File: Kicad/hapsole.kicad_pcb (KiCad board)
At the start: 2 copper layers, 39.3 x 36.8 mm, 63 parts, among them J1 2171790001, J2 Conn_01x02_Socket, J3 Conn_01x02_Socket, Q1 PMOS, SW1 SW_SPST, U1 DA7281-00FV2, U2 DA7281-00FV2, U3 nRF52840, U4 LSM6DS3TR-C, U5 BQ25100YFPR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

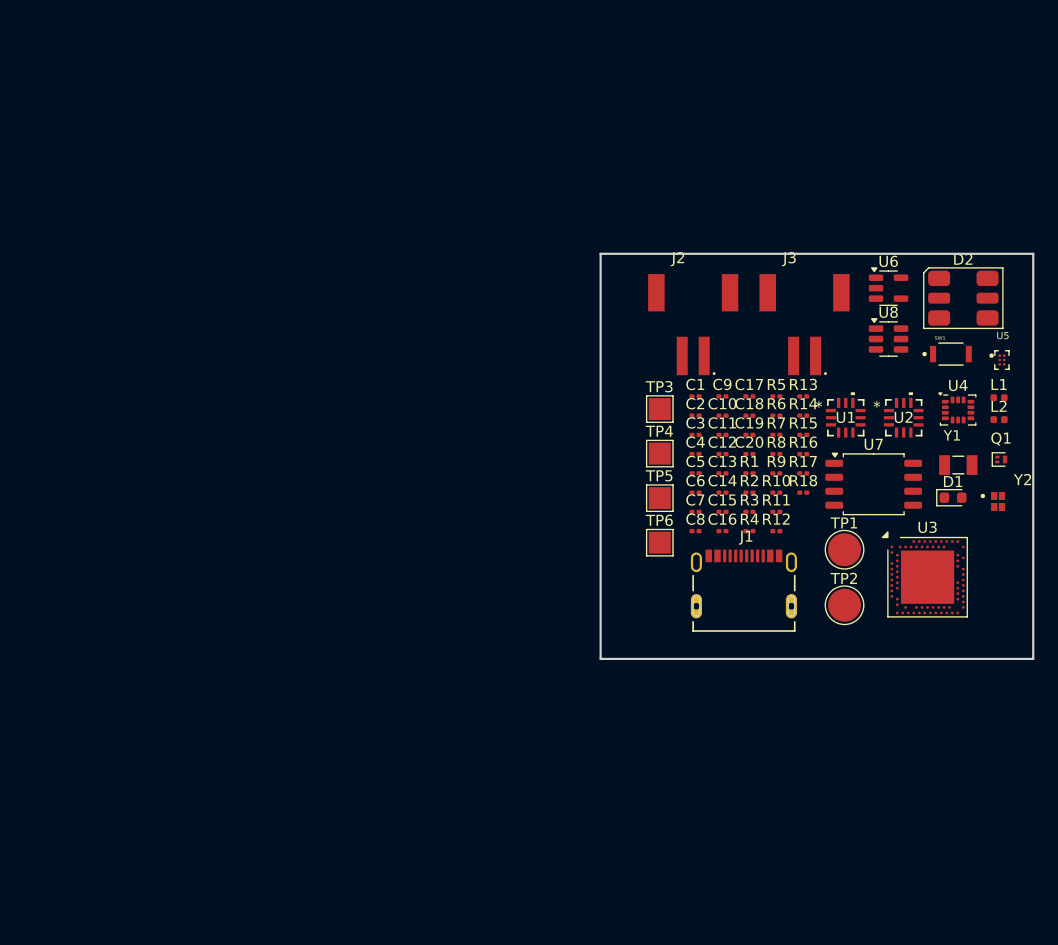
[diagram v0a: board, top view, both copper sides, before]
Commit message: placed the components in PCB & started routing
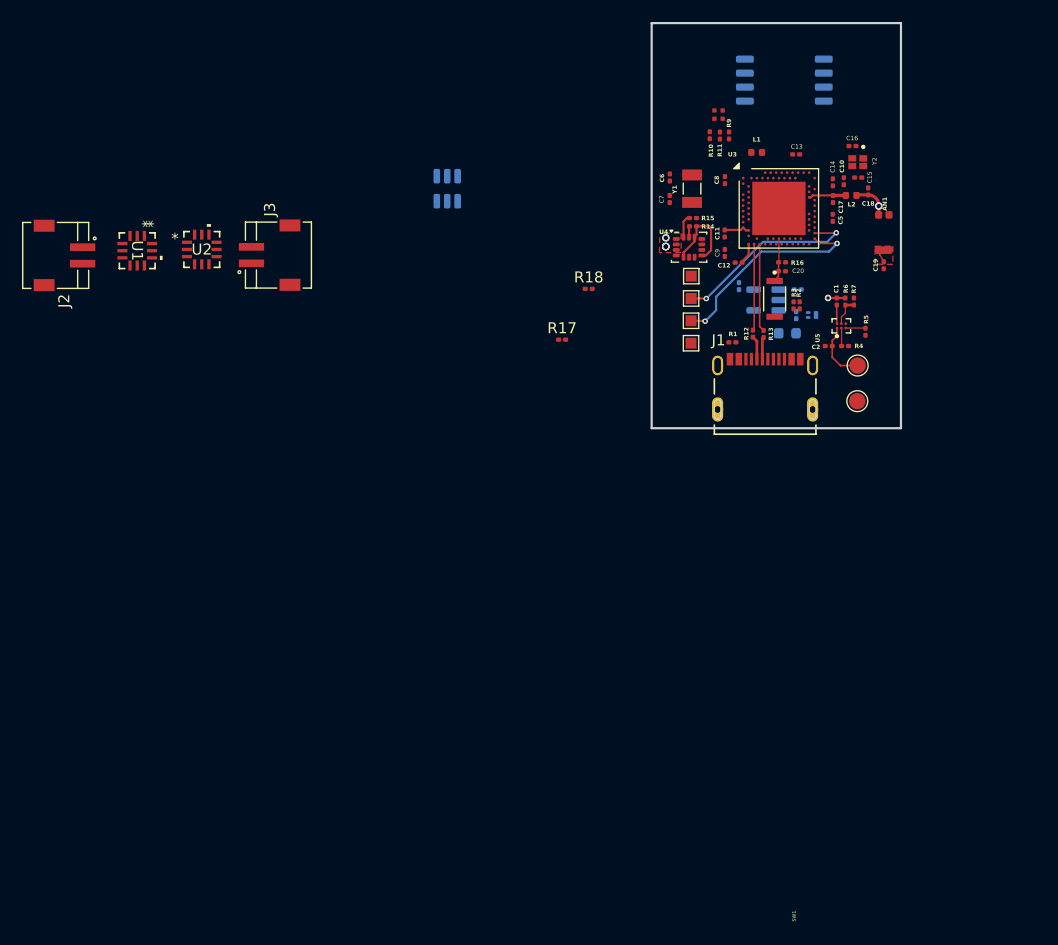
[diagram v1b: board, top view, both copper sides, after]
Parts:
- removed D2: Inolux_IN-P55TATRGB, LED_SMD:LED_Inolux_IN-P55TATRGB_PLCC6_5.0x5.5mm_P1.8mm
- added AN1: ~, Arjun_Custom:Ant, F.Cu at (117.7, 104.2)
- added LED1: ~, Arjun_Custom:RGB_LED_P4_1010, F.Cu at (102.9, 93.5)
- C3, C4, D1, Q1, R8, U6, U7, U8: moved to B.Cu
- J2, J3: footprint Arjun_Custom:JST_S2B-PH-SM4-TB -> Arjun_Custom:JST_S2B-ZR-SM4A-TF
- TP1, TP2: footprint TestPoint:TestPoint_Pad_D3.0mm -> TestPoint:TestPoint_Pad_D1.5mm
- TP3, TP4, TP5, TP6: footprint TestPoint:TestPoint_Pad_2.0x2.0mm -> TestPoint:TestPoint_Pad_1.0x1.0mm
- moved U1 66.2 mm to (49.9, 106.0), turned to -90 degrees
- moved U2 65.6 mm to (55.8, 105.9)
- moved J2 56.3 mm to (45.0, 106.4), turned to 90 degrees
- moved J3 51.1 mm to (60.3, 106.4), turned to -90 degrees
- moved U8 42.4 mm to (78.1, 100.4), turned to 90 degrees
- moved U7 37.6 mm to (108.8, 90.5), turned to 180 degrees
- moved C16 37.0 mm to (115.0, 96.5), turned to 180 degrees
- moved U3 36.2 mm to (108.3, 102.2)
- moved Y1 34.9 mm to (100.4, 100.4), turned to 90 degrees
- moved R11 34.6 mm to (102.9, 95.5), turned to 90 degrees
- moved Y2 33.4 mm to (115.4, 98.0), turned to -90 degrees
- moved R10 33.1 mm to (102.0, 95.5), turned to 90 degrees
- moved C15 32.8 mm to (115.5, 99.4)
- moved C8 32.0 mm to (103.4, 99.6), turned to 90 degrees
- moved L1 31.4 mm to (106.2, 97.1)
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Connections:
- U1 pad 5: Net-(J2-Pin_2) -> Net-(J2-Pin_1)
- U1 pad 8: Net-(J2-Pin_1) -> Net-(J2-Pin_2)
- U2 pad 5: Net-(J3-Pin_2) -> Net-(J3-Pin_1)
- U2 pad 8: Net-(J3-Pin_1) -> Net-(J3-Pin_2)
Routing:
- net /SWDIO: track 0.00 -> 19.1 mm, vias 0 -> 2
- net /SWDCLK: track 0.00 -> 17.6 mm, vias 0 -> 2
- net Net-(U3-D+): track 0.00 -> 8.00 mm
- net Net-(U3-D-): track 0.00 -> 7.87 mm
- net /6D_PWR: track 0.00 -> 7.72 mm
- net /VBAT: track 0.00 -> 5.47 mm
- net /RESET: track 0.00 -> 4.02 mm
- net /VBUS: track 0.00 -> 3.62 mm
- net Net-(U3-ANT): track 0.00 -> 3.41 mm
- net Net-(AN1-S): track 0.00 -> 3.32 mm, vias 0 -> 1
- net Net-(U5-ISET): track 0.00 -> 2.63 mm
- net /3V3: track 0.00 -> 2.34 mm
- net /USB_D-: track 0.00 -> 2.15 mm
- net /INTERNAL_I2C_SDA: track 0.00 -> 2.10 mm
- net /USB_D+: track 0.00 -> 2.02 mm
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- added copper zone on In2.Cu, net /3V3
- added copper zone on F.Cu, net GND
- added copper zone on In1.Cu, net GND
- added copper zone on F.Cu, net Net-(AN1-Pad3)
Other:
- board size 39.3 x 36.8 mm -> 22.7 x 36.8 mm
- copper layers 2 -> 4

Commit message: added library
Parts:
- U3: footprint Package_DFN_QFN:Nordic_AQFN-73-1EP_7x7mm_P0.5mm -> Arjun_Custom:NRF52840
- moved U3 3.76 mm to (107.4, 98.5)
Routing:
- net /6D_INT1: track 0.00 -> 10.2 mm, vias 0 -> 2
- net /6D_PWR: track 7.72 -> 13.4 mm
- net /3V3: track 2.34 -> 3.79 mm, vias 0 -> 2
- net Net-(AN1-S): vias 1 -> 0

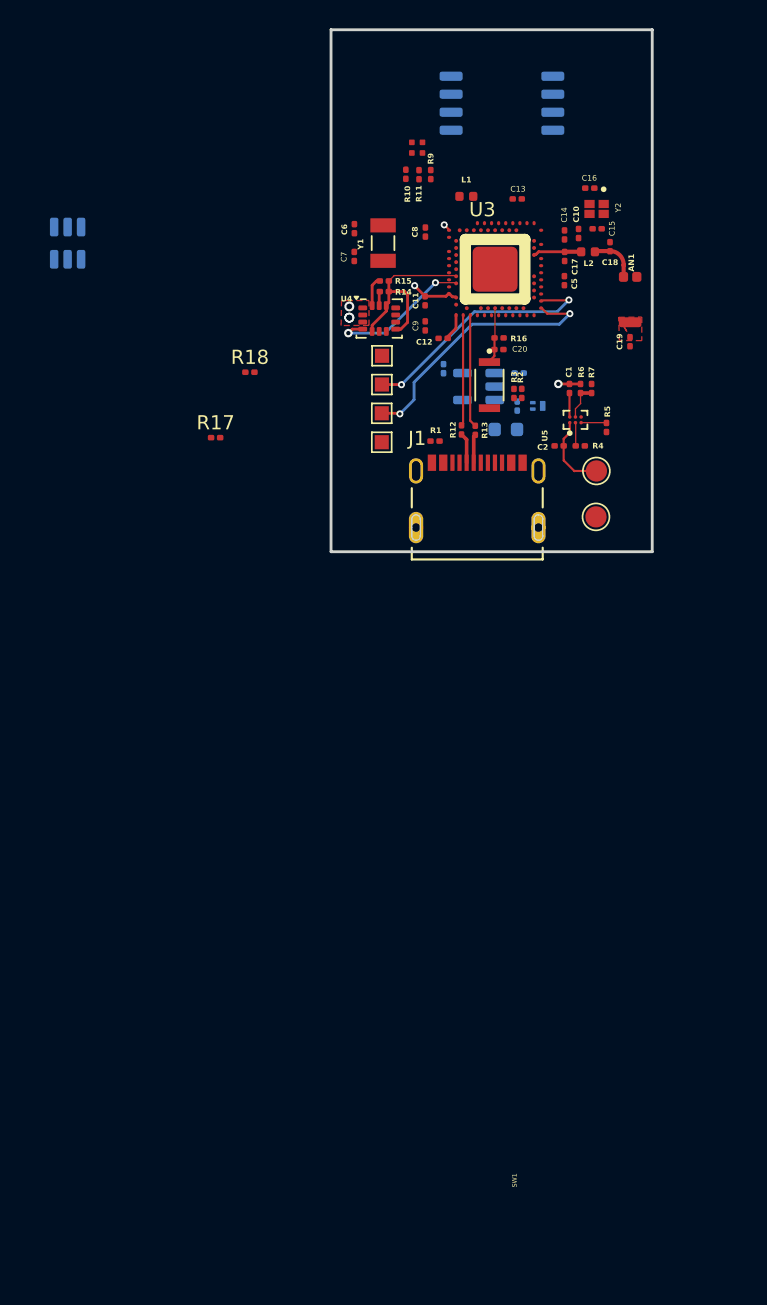
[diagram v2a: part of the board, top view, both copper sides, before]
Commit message: Resized and rearranged components placement
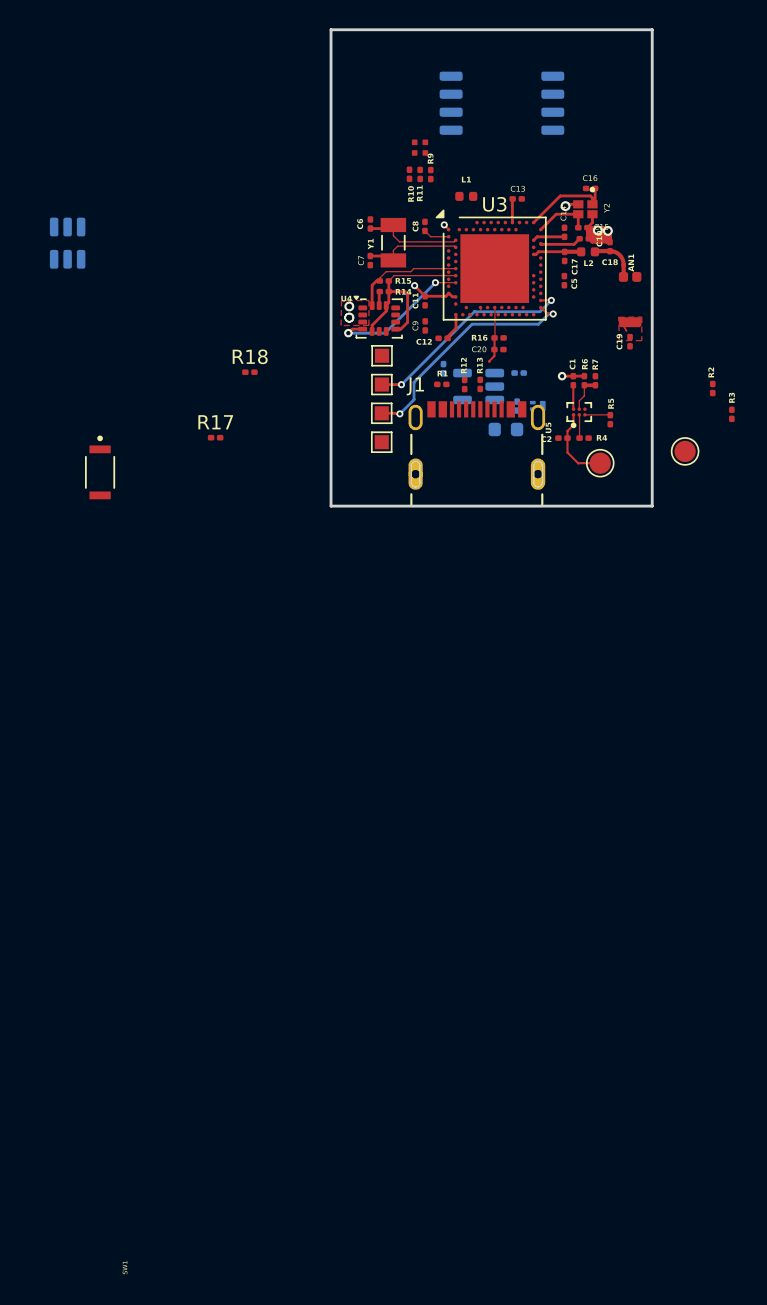
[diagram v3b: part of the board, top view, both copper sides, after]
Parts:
- U3: footprint Arjun_Custom:NRF52840 -> Package_DFN_QFN:Nordic_AQFN-73-1EP_7x7mm_P0.5mm
- moved SW1 28.2 mm to (80.4, 116.5)
- moved R3 15.5 mm to (125.0, 112.5)
- moved R2 13.5 mm to (123.6, 110.6)
- moved TP2 7.80 mm to (121.7, 115.1)
- moved R1 4.03 mm to (104.5, 110.3)
- moved J1 3.77 mm to (107.0, 115.5)
- moved U3 3.76 mm to (108.3, 102.2)
- moved R13 3.26 mm to (107.2, 110.3)
- moved R12 3.21 mm to (106.1, 110.3)
- moved C6 1.18 mm to (99.5, 99.0), turned to -90 degrees
- moved C7 1.17 mm to (99.5, 101.6), turned to 90 degrees
- moved C15 1.01 mm to (114.5, 99.3)
- moved Y2 0.79 mm to (114.7, 98.0)
- moved Y1 0.73 mm to (101.1, 100.3)
- moved C2 0.61 mm to (113.1, 114.1)
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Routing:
- net GND: track 1.57 -> 22.0 mm, vias 4 -> 7
- net Net-(U3-D+): track 8.00 -> 0.06 mm
- net Net-(U3-D-): track 7.87 -> 0.00 mm
- net Net-(U3-XL1/P0.00): track 0.00 -> 7.23 mm
- net Net-(U3-XL2/P0.01): track 0.00 -> 7.04 mm
- net Net-(U3-XC2): track 0.00 -> 6.64 mm
- net /INTERNAL_I2C_SDA: track 2.10 -> 7.94 mm
- net Net-(U3-XC1): track 0.00 -> 4.05 mm
- net /DEC4-6: track 0.00 -> 2.93 mm
- net /SWDCLK: track 17.6 -> 15.1 mm
- net /SWDIO: track 19.1 -> 16.8 mm
- net Net-(U3-DEC3): track 0.00 -> 2.28 mm
- net /USB_D-: track 2.15 -> 0.00 mm
- net /USB_D+: track 2.02 -> 0.00 mm
- net Net-(U3-DEC1): track 0.00 -> 1.84 mm
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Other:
- board size 22.7 x 36.8 mm -> 22.7 x 33.6 mm

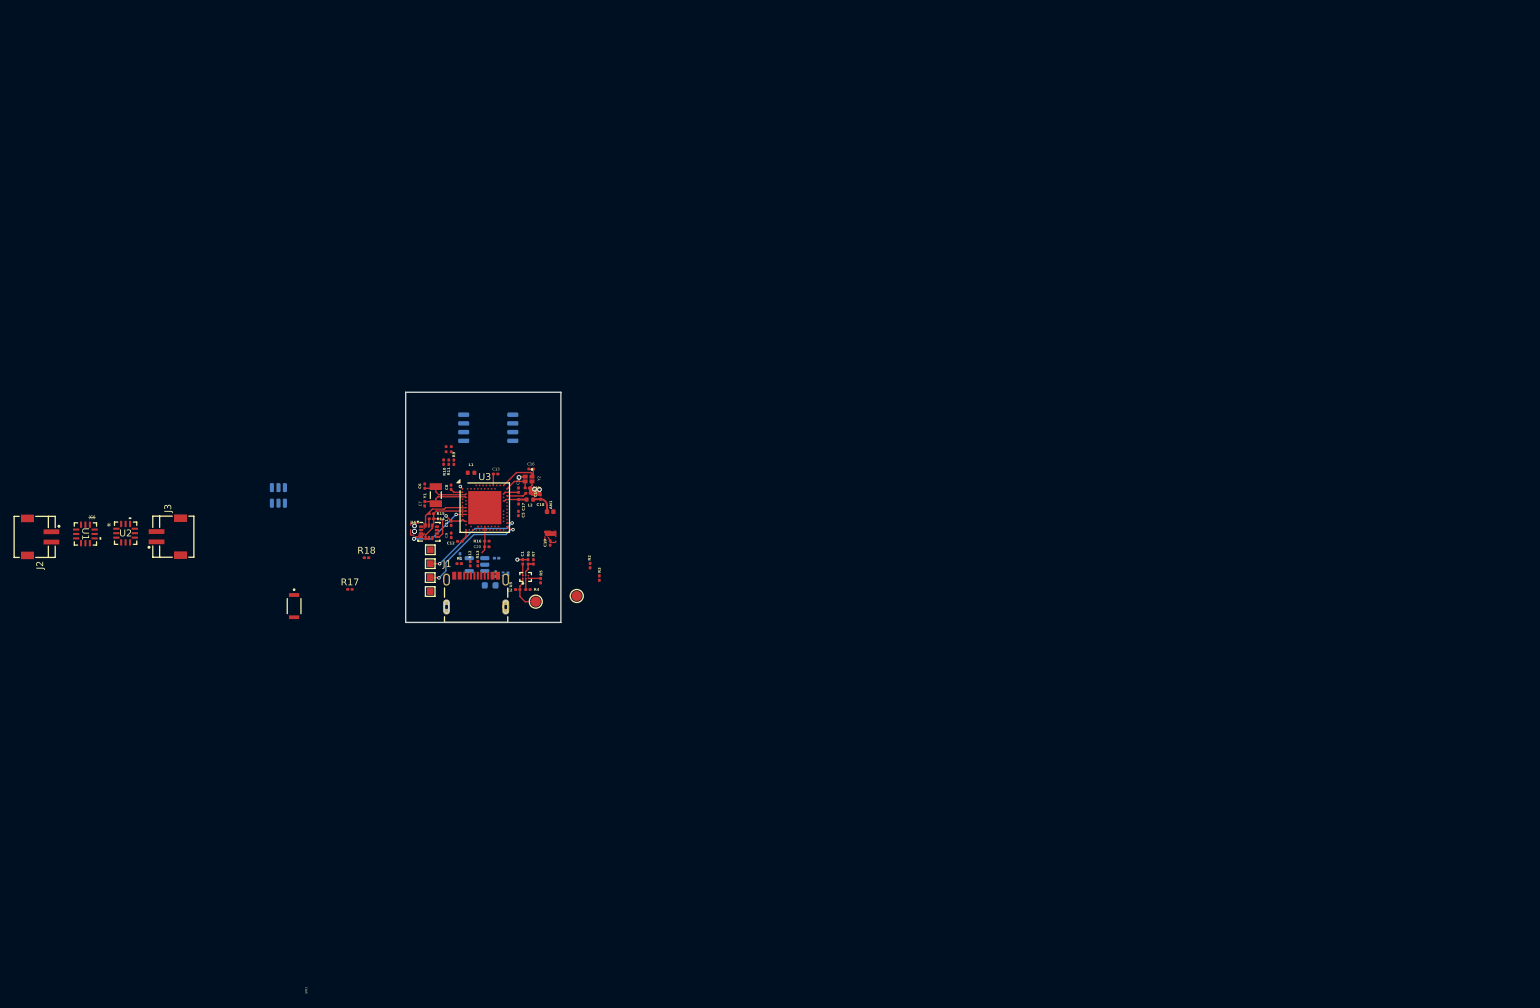
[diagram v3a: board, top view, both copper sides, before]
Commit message: Deleted the pcb design and start from the scratch
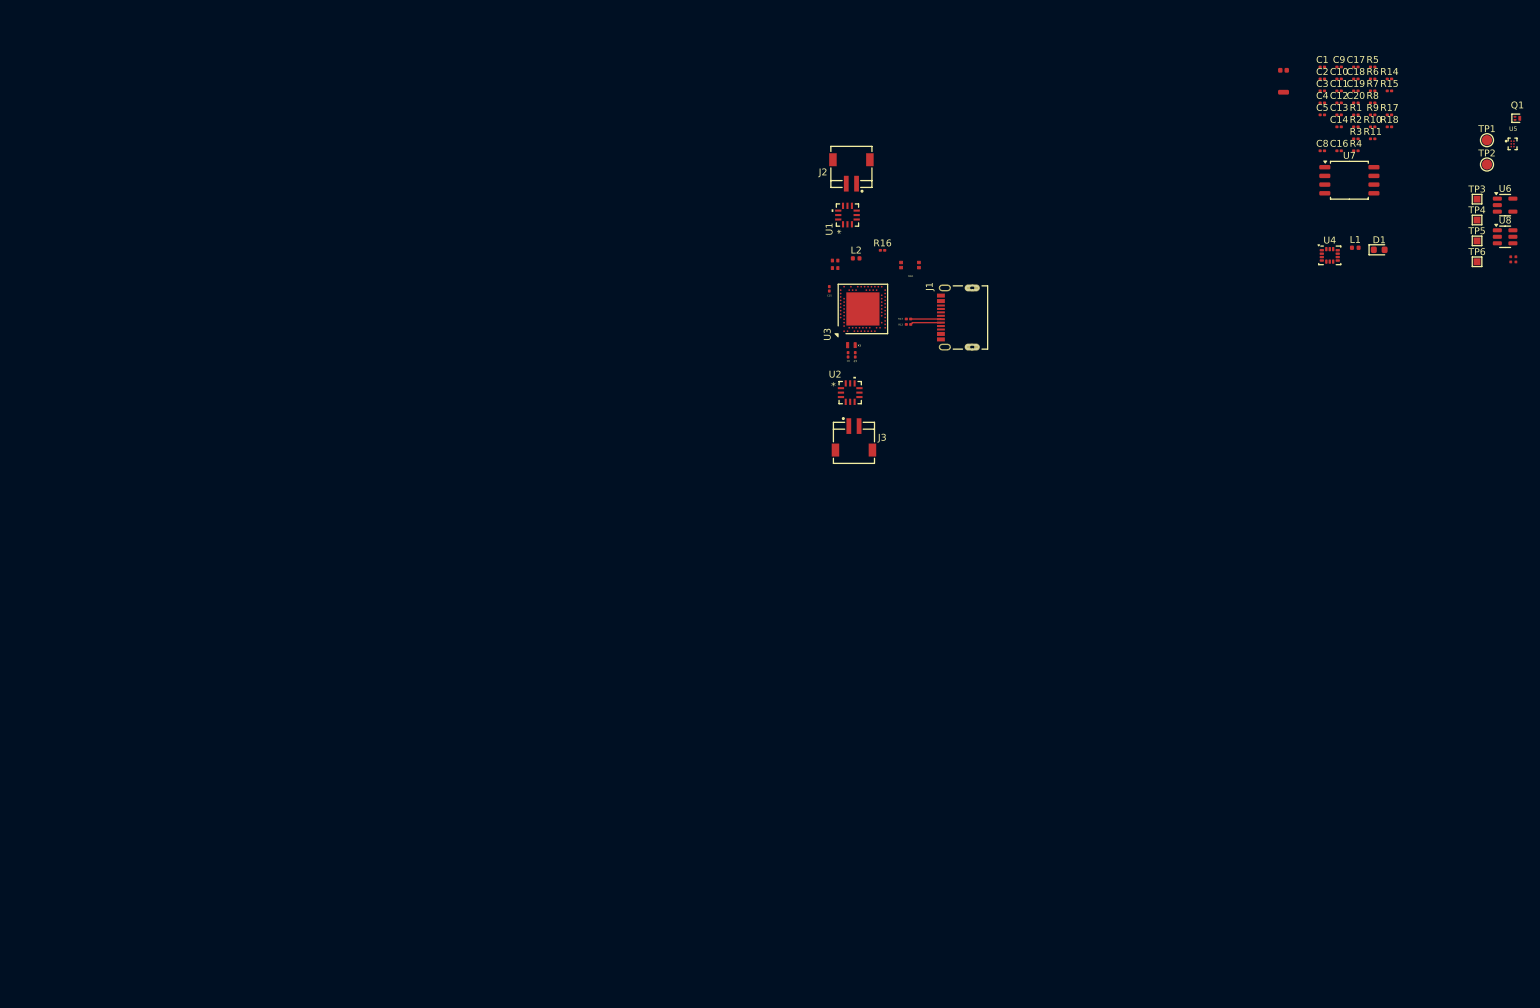
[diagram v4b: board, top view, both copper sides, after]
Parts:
- removed Y1: 32.768Khz, Arjun_Custom:XTAL_FC-135_32.7680KA-A0
- removed Y2: ~, Arjun_Custom:XTAL_ABM12W-40.0000MHZ-6-D1X-T3
- added X1: 32.768Khz, Hapsole_Custom:FC135, F.Cu at (161.8, 78.4)
- added X2: 32MHz, Hapsole_Custom:XC, F.Cu at (159.4, 66.6)
- AN1: footprint Arjun_Custom:Ant -> Hapsole_Custom:ANT
- C3, C4, D1, Q1, R8, U6, U7, U8: moved to F.Cu
- J1: footprint Arjun_Custom:MOLEX_2171790001 -> Hapsole_Custom:MOLEX_2171790001
- J2, J3: footprint Arjun_Custom:JST_S2B-ZR-SM4A-TF -> Hapsole_Custom:JST_S2B-ZR-SM4A-TF
- LED1: footprint Arjun_Custom:RGB_LED_P4_1010 -> Hapsole_Custom:RGB_LED
- SW1: value SW_SPST -> ~; footprint Arjun_Custom:SW_EVP-AWED4A -> Hapsole_Custom:DPST
- U1, U2: footprint Arjun_Custom:DA7281-00FV2_DIL -> Hapsole_Custom:DA7281-00FV2_DIL
- U5: footprint Arjun_Custom:BGA6N40P3X2_157X88X50N -> Hapsole_Custom:BGA6N40P3X2_157X88X50N
- moved U8 183.1 mm to (257.3, 62.6), turned to 0 degrees
- moved R17 166.9 mm to (240.4, 44.8)
- moved TP3 163.3 mm to (253.2, 57.1)
- moved R18 162.1 mm to (240.4, 46.5)
- moved Q1 162.1 mm to (259.1, 45.3)
- moved TP4 160.3 mm to (253.2, 60.1)
- moved TP5 160.0 mm to (253.2, 63.2)
- moved TP6 159.7 mm to (253.2, 66.2)
- moved U6 159.1 mm to (257.3, 58.0), turned to 0 degrees
- moved LED1 158.0 mm to (258.5, 65.9)
- moved U5 157.4 mm to (258.4, 49.0), turned to 0 degrees
- moved TP1 154.4 mm to (254.7, 48.5)
- moved R14 154.0 mm to (240.4, 39.5)
- moved R15 153.0 mm to (240.4, 41.3)
- moved TP2 147.1 mm to (254.7, 52.0)
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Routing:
- net GND: track 22.0 -> 0.00 mm, vias 7 -> 0
- net /SWDIO: track 16.8 -> 0.00 mm, vias 2 -> 0
- net /SWDCLK: track 15.1 -> 0.00 mm, vias 2 -> 0
- net /6D_PWR: track 13.4 -> 0.00 mm
- net /6D_INT1: track 10.2 -> 0.00 mm, vias 2 -> 0
- net /INTERNAL_I2C_SDA: track 7.94 -> 0.00 mm
- net Net-(U3-XL1/P0.00): track 7.23 -> 0.00 mm
- net Net-(U3-XL2/P0.01): track 7.04 -> 0.00 mm
- net Net-(U3-XC2): track 6.64 -> 0.00 mm
- net /VBAT: track 5.47 -> 0.00 mm
- net /USB_D-: track 0.00 -> 4.52 mm
- net /USB_D+: track 0.00 -> 4.43 mm
- net Net-(U3-XC1): track 4.05 -> 0.00 mm
- net /RESET: track 4.02 -> 0.00 mm
- net /3V3: track 3.79 -> 0.00 mm, vias 2 -> 0
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- removed copper zone on In2.Cu, net /3V3
- removed copper zone on F.Cu, net GND
- removed copper zone on In1.Cu, net GND
- removed copper zone on F.Cu, net Net-(AN1-Pad3)
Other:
- board size 22.7 x 33.6 mm -> 1.8 x 9.2 mm

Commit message: Arranged the components
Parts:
- moved U5 97.3 mm to (166.5, 80.9), turned to 90 degrees
- moved U6 89.7 mm to (170.6, 81.0)
- moved R6 82.2 mm to (166.2, 79.7)
- moved R5 82.2 mm to (168.0, 80.9), turned to -90 degrees
- moved R7 80.1 mm to (167.7, 79.7), turned to 180 degrees
- moved C13 79.4 mm to (158.6, 72.2), turned to -90 degrees
- moved R2 78.7 mm to (164.3, 80.0), turned to 90 degrees
- moved C2 78.4 mm to (164.3, 81.5), turned to -90 degrees
- moved L1 78.0 mm to (158.4, 76.7), turned to 90 degrees
- moved C1 78.0 mm to (165.1, 80.0), turned to -90 degrees
- moved C16 77.7 mm to (158.2, 70.9), turned to 180 degrees
- moved C9 77.1 mm to (167.3, 78.0)
- moved C11 76.8 mm to (165.6, 78.0)
- moved C10 76.8 mm to (161.6, 67.9), turned to 90 degrees
- moved C8 76.2 mm to (159.7, 78.1), turned to 180 degrees
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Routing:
- net /USB_D-: track 4.52 -> 0.00 mm
- net /USB_D+: track 4.43 -> 0.04 mm
- net Net-(D1-K): track 0.00 -> 3.72 mm
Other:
- board size 1.8 x 9.2 mm -> 33.5 x 22.6 mm
